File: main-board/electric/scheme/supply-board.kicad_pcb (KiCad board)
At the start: 2 copper layers, 85 x 56 mm, 139 parts, among them K1 CONN_3, P1 PWR-IN, P10 TST, P11 TST, P12 PWR-IN, P13 CONN_4, P14 PWR-IN, P16 TST, P17 TST, P18 TST, P19 TST, P2 PWR-IN, P3 CONN_4, P4 cross board conn, P5 PWR-IN, P6 TST, P7 TST, P8 TST, P9 CONN_3X2, Q1 BC847, Q10 MOS_N, Q11 MOS_P, Q12 MOS_P, Q2 BC847, Q3 BC847, Q4 MOS_P, Q5 BC847, Q6 BC857, Q7 BC847, Q8 BC857, Q9 BC847, U1 NCP3063, U2 L293, U3 MINI-USB-B, X1 8MHz

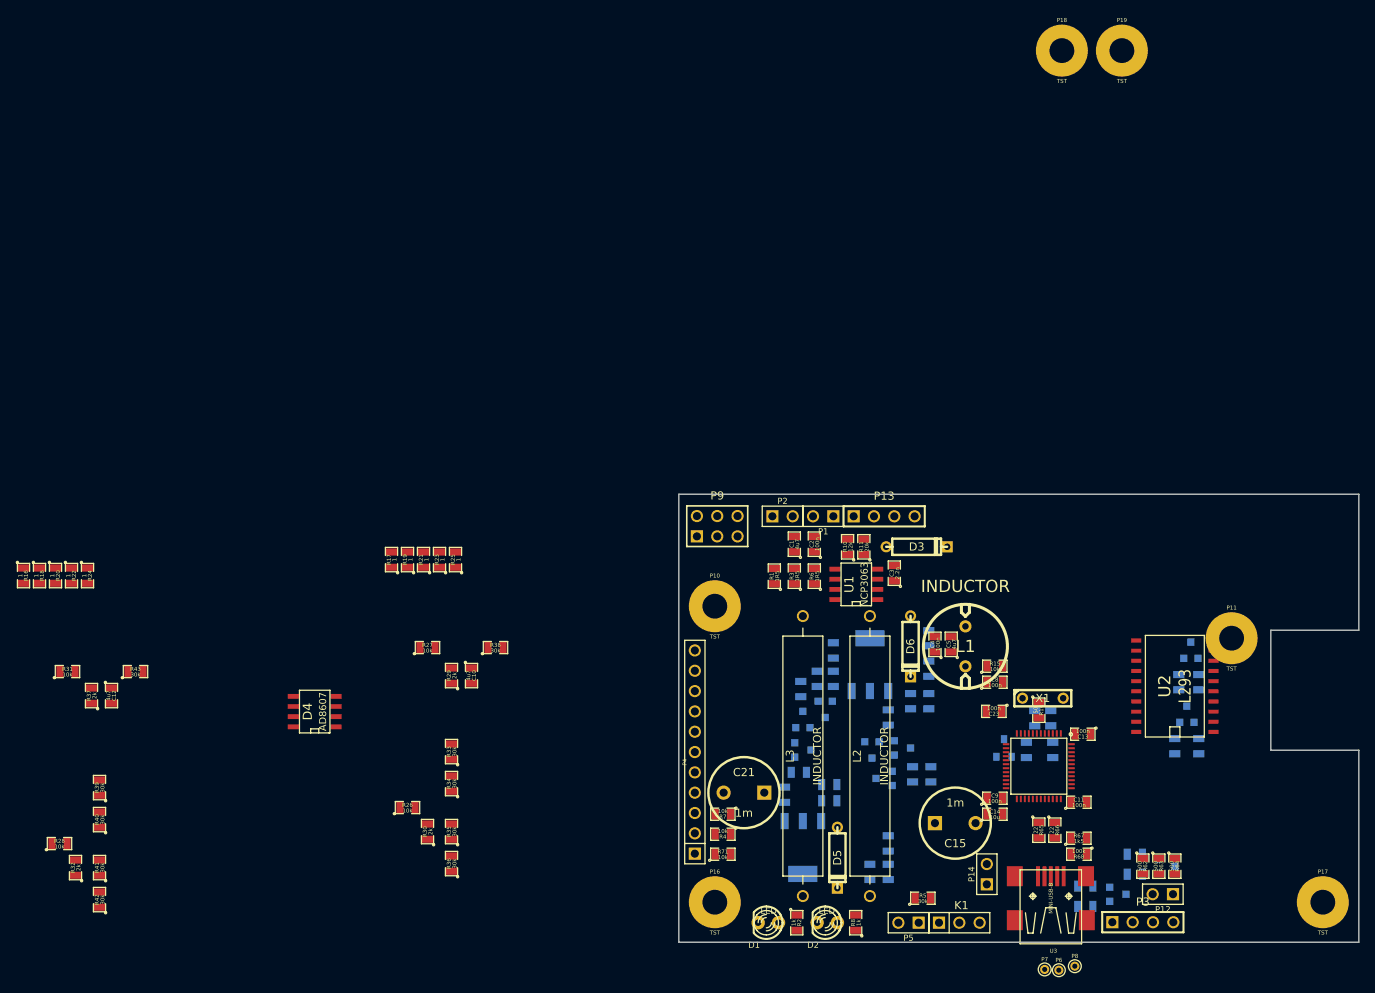
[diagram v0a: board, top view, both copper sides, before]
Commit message: Composed current measure circuit outside of the board.
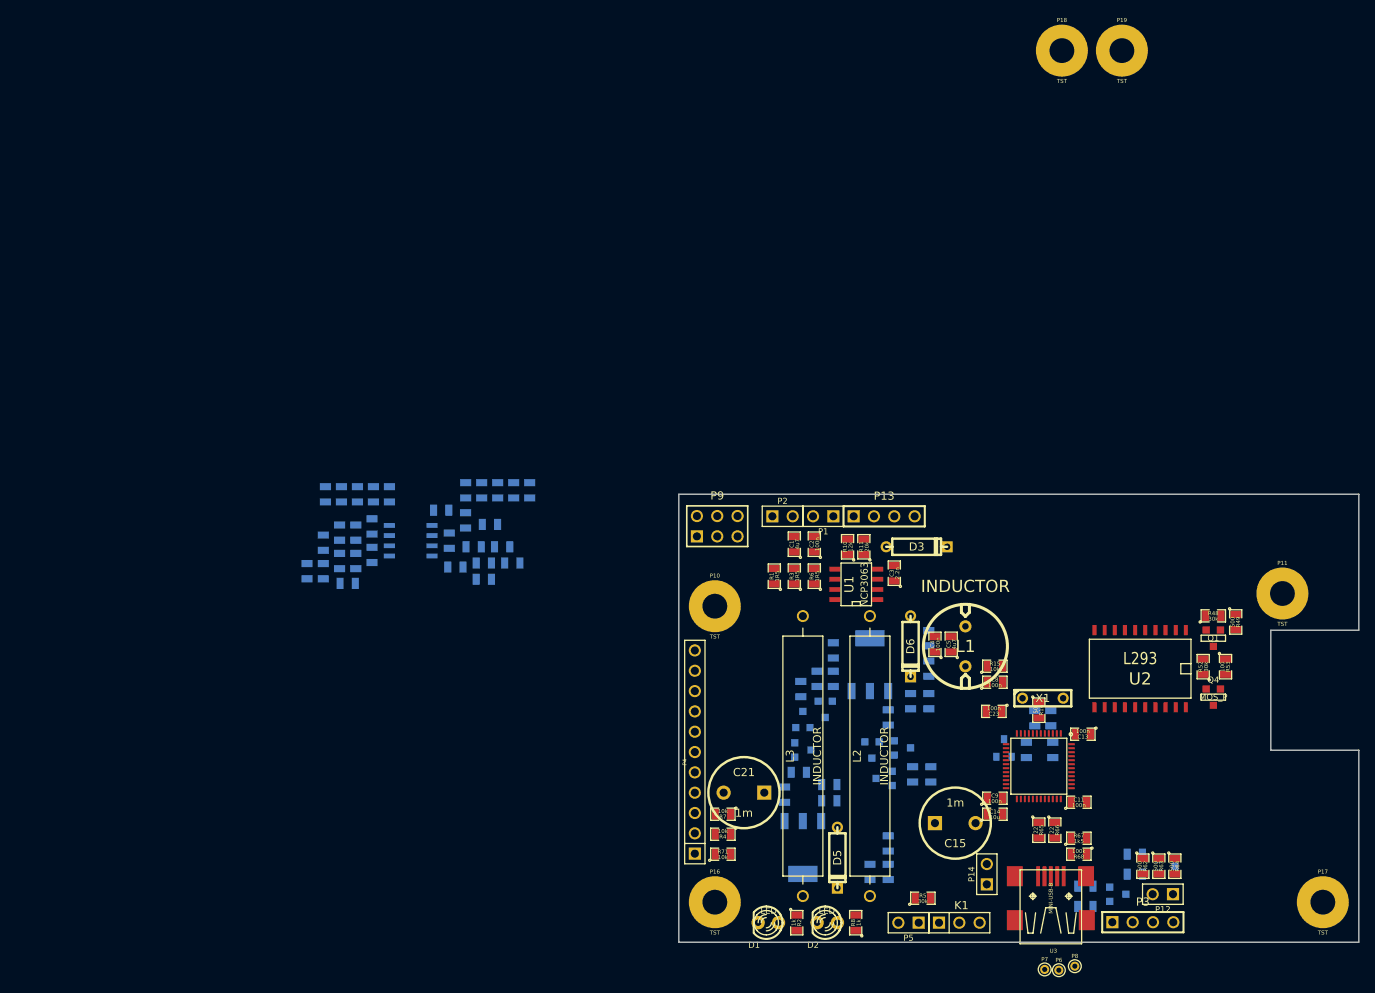
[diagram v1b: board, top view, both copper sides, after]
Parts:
- C10, C12, D4, R16, R17, R18, R19, R20, R21, R22, R23, R24, R25, R26, R27, R28, R29, R30, R31, R32, R33, R34, R35, R36, R37, R38, R39, R40, R41, R42, R43: moved to B.Cu
- Q1, Q4, R48, R49, R52, R53: moved to F.Cu
- moved R32 51.9 mm to (103.1, 133.3)
- moved R42 50.2 mm to (102.1, 136.1), turned to 180 degrees
- moved R28 50.0 mm to (99.1, 131.1), turned to 270 degrees
- moved R41 48.7 mm to (101.1, 133.3)
- moved R16 46.9 mm to (107.3, 125.0)
- moved R18 43.0 mm to (105.3, 125.0)
- moved R40 41.8 mm to (99.1, 134.6), turned to 270 degrees
- moved R36 40.1 mm to (121.4, 131.6), turned to 180 degrees
- moved R31 40.0 mm to (103.1, 129.8), turned to 270 degrees
- moved R20 39.1 mm to (103.3, 125.0)
- moved R39 37.5 mm to (97.0, 134.6)
- moved R37 37.1 mm to (101.1, 129.8), turned to 270 degrees
- moved C12 37.0 mm to (105.2, 132.6)
- moved R35 35.7 mm to (117.9, 131.6), turned to 180 degrees
- moved R22 35.2 mm to (101.3, 125.0)
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
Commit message: Changed USB power from "batt+" to "solar+".
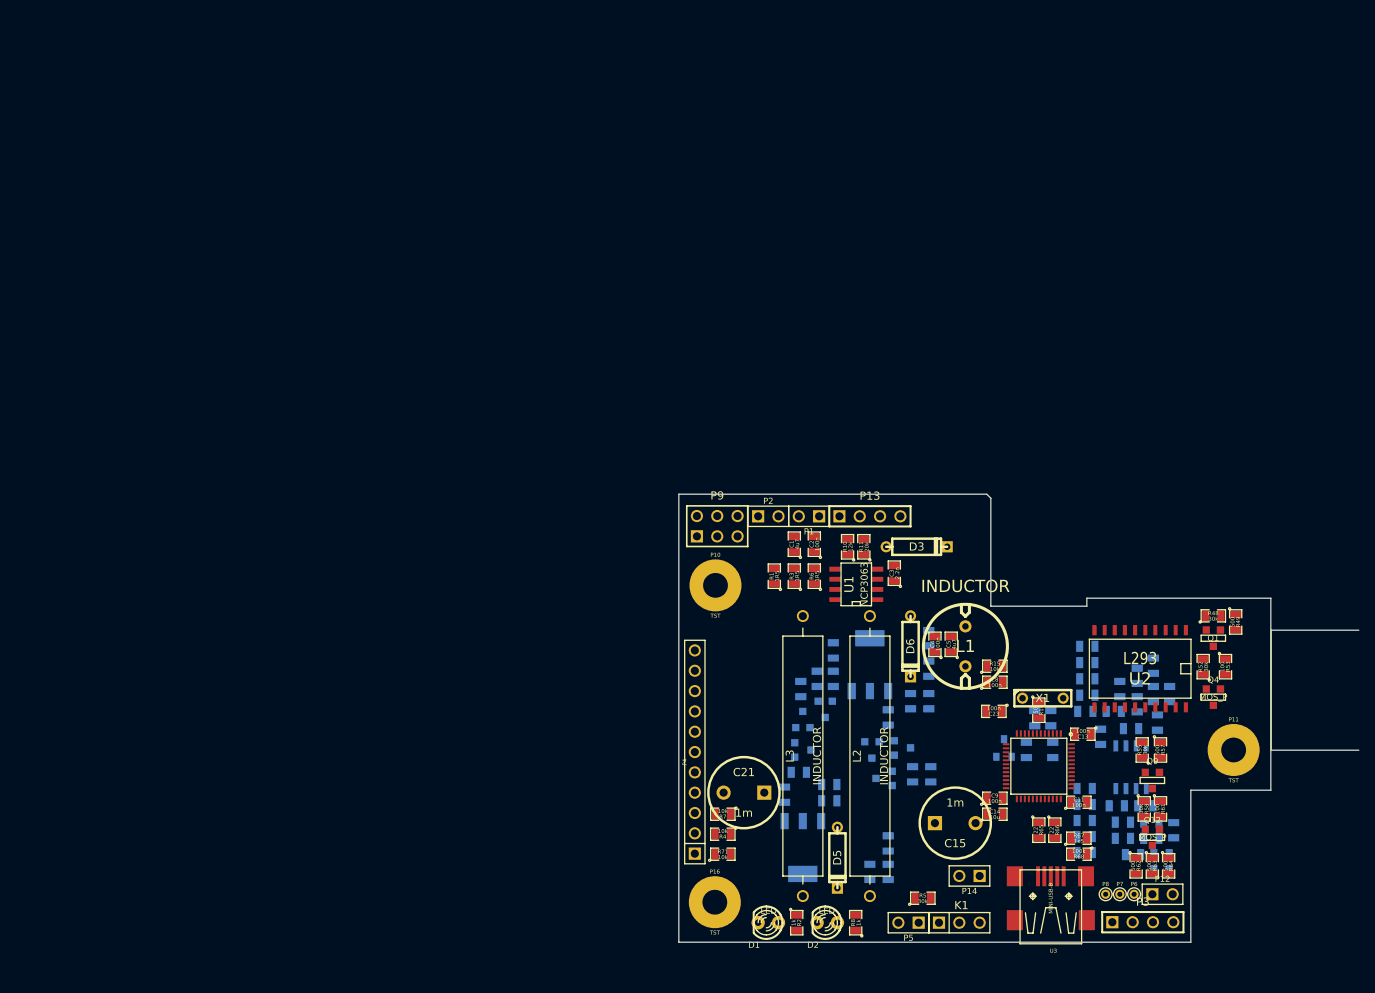
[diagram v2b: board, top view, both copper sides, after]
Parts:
- removed P17, P18, P19: TST, m3-screw-hole
- Q12, Q9, R55, R57, R58, R61: moved to F.Cu
- moved R39 113.2 mm to (203.8, 172.1), turned to 180 degrees
- moved R40 110.6 mm to (203.8, 170.1), turned to 0 degrees
- moved R28 108.5 mm to (200.3, 170.1), turned to 0 degrees
- moved R42 107.8 mm to (205.4, 167.0), turned to 270 degrees
- moved R41 107.2 mm to (202.6, 168.0), turned to 180 degrees
- moved R37 105.1 mm to (199.0, 168.0), turned to 0 degrees
- moved R24 104.9 mm to (194.2, 169.8), turned to 0 degrees
- moved R32 104.7 mm to (202.6, 166.0), turned to 180 degrees
- moved R31 102.5 mm to (199.0, 166.0), turned to 0 degrees
- moved R22 102.3 mm to (194.2, 167.8), turned to 0 degrees
- moved C12 101.6 mm to (201.8, 164.0), turned to 0 degrees
- moved R20 99.6 mm to (194.2, 165.8), turned to 0 degrees
- moved R43 99.4 mm to (198.2, 164.0), turned to 0 degrees
- moved R18 97.0 mm to (194.2, 163.8), turned to 0 degrees
- moved D4 94.4 mm to (200.0, 159.1), turned to 0 degrees
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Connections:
- P14 pad 2: +6V -> /solar+
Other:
- outline, holes or cut-outs redrawn
- net class Default: trace_width 0.2 -> 0.25

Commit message: Routing.
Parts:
- moved P6 5.03 mm to (196.8, 171.4)
- moved C15 3.61 mm to (174.6, 167.3)
- moved P7 2.51 mm to (196.8, 173.2)
- moved R8 1.27 mm to (166.9, 178.6), turned to 180 degrees
- moved R14 1.06 mm to (188.5, 150.9)
- moved X1 1.02 mm to (189.0, 149.5)
- moved D1 0.76 mm to (153.9, 178.6)
- moved D2 0.76 mm to (162.8, 178.6)
- moved C23 0.68 mm to (183.4, 151.7), turned to 0 degrees
- moved R67 0.62 mm to (193.5, 167.4)
- moved R5 0.53 mm to (173.5, 175.4), turned to 90 degrees
- moved R2 0.25 mm to (158.0, 178.6), turned to 180 degrees
- moved C9 0.06 mm to (183.0, 162.9), turned to 180 degrees
- turned C14 to 180 degrees
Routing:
- net GND: track 0.00 -> 83.6 mm
- net +6V: track 0.00 -> 19.1 mm
- net /swd-io: track 0.00 -> 14.2 mm
- net /swd-clk: track 0.00 -> 13.4 mm
- net N-0000044: track 0.00 -> 10.1 mm
- net /usb-connected: track 0.00 -> 8.59 mm
- net N-0000012: track 0.00 -> 7.34 mm
- net N-0000021: track 0.00 -> 6.67 mm
- net N-0000022: track 0.00 -> 5.65 mm
- net N-0000013: track 0.00 -> 5.09 mm
- net N-0000084: track 0.00 -> 4.38 mm
- net N-0000033: track 0.00 -> 4.12 mm
- net VDD: track 0.00 -> 4.01 mm
- net N-0000023: track 0.00 -> 3.62 mm
- net /d+: track 0.00 -> 3.26 mm
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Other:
- board size 85 x 56 mm -> 74 x 56 mm

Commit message: Routing...
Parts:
- moved C23 1.23 mm to (184.6, 152.0)
- moved C12 0.76 mm to (202.6, 164.0)
- moved R43 0.76 mm to (199.0, 164.0), turned to 180 degrees
- turned C13 to 0 degrees
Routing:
- net +6V: track 19.1 -> 103.6 mm
- net GND: track 83.6 -> 157.3 mm
- net /buck-out-5v: track 2.54 -> 53.8 mm
- net /solar+: track 0.00 -> 39.2 mm
- net N-0000026: track 0.00 -> 23.4 mm
- net VDD: track 4.01 -> 21.4 mm
- net N-0000027: track 0.00 -> 13.7 mm
- net /in2+: track 0.00 -> 11.5 mm
- net /solar: track 0.00 -> 11.2 mm
- net /boost+: track 0.00 -> 11.0 mm
- net N-0000017: track 2.00 -> 10.3 mm
- net /in2-: track 0.00 -> 7.90 mm
- net N-0000019: track 0.00 -> 7.00 mm
- net N-000007: track 0.00 -> 5.09 mm
- net N-0000034: track 0.00 -> 5.04 mm
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
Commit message: Routing...
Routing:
- net N-000008: track 0.00 -> 12.9 mm
- net /in1+: track 0.00 -> 10.9 mm
- net GND: track 157.3 -> 167.8 mm
- net /buck+: track 0.00 -> 9.88 mm
- net /in1-: track 0.00 -> 9.36 mm
- net +6V: track 103.6 -> 111.8 mm
- net N-0000014: track 0.00 -> 5.38 mm
- net N-0000020: track 2.31 -> 5.52 mm
- net N-0000019: track 7.00 -> 10.2 mm
- net /buck-current: track 0.00 -> 1.98 mm
- net N-0000059: track 0.00 -> 1.65 mm
- net N-0000058: track 0.00 -> 1.65 mm

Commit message: Routing...
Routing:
- net GND: track 167.8 -> 257.9 mm
- net /buck+: track 9.88 -> 20.0 mm
- net /buck-out-5v: track 53.8 -> 63.3 mm
- net N-000003: track 4.73 -> 14.1 mm
- net N-000007: track 5.09 -> 14.5 mm
- net N-000002: track 0.00 -> 8.99 mm
- net N-000004: track 0.00 -> 8.43 mm
- net +6V: track 111.8 -> 118.5 mm
- net /solar: track 11.2 -> 15.6 mm
- net N-000006: track 0.00 -> 4.24 mm
- net VDD: track 21.4 -> 24.1 mm
- net N-000005: track 0.00 -> 2.40 mm
- net N-0000015: track 0.00 -> 2.35 mm
- net N-000001: track 0.00 -> 2.35 mm
- net /batt-volt: track 0.00 -> 1.91 mm
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
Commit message: Routing...
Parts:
- moved U2 13.0 mm to (206.5, 135.0), turned to 90 degrees
- moved R48 11.8 mm to (201.5, 147.9), turned to 90 degrees
- moved R49 11.7 mm to (202.2, 145.1), turned to 0 degrees
- moved Q1 7.82 mm to (204.3, 147.9), turned to 90 degrees
- moved R53 4.03 mm to (207.8, 146.4), turned to 0 degrees
- moved R52 2.92 mm to (207.8, 149.2), turned to 180 degrees
- moved Q4 2.76 mm to (211.6, 147.9), turned to 90 degrees
- moved C14 1.21 mm to (181.8, 164.9)
- moved R65 0.56 mm to (188.8, 167.5)
- moved R66 0.50 mm to (190.5, 167.5)
- moved R28 0.38 mm to (200.3, 170.4)
- moved R39 0.25 mm to (203.8, 172.3)
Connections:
- stm1 pad 25: /light -> (no net)
- stm1 pad 26: /moto4 -> /led1
- stm1 pad 27: /moto3 -> /led2
- stm1 pad 29: (no net) -> /usb-connected
- stm1 pad 3: /led1 -> /moto4
- stm1 pad 38: /usb-connected -> (no net)
- stm1 pad 4: /led2 -> /moto3
- stm1 pad 41: (no net) -> /light
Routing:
- net GND: track 257.9 -> 363.1 mm
- net /wakeup: track 0.00 -> 40.3 mm
- net /sda-int: track 2.59 -> 42.9 mm, vias 0 -> 2
- net /scl-int: track 2.61 -> 42.1 mm, vias 0 -> 2
- net /moto-en: track 1.92 -> 39.7 mm, vias 0 -> 2
- net /led1: track 0.00 -> 35.9 mm
- net /moto3: track 0.00 -> 33.2 mm
- net /buck-pwm: track 0.00 -> 32.8 mm, vias 0 -> 1
- net /led2: track 0.00 -> 28.1 mm
- net /rx: track 0.00 -> 27.4 mm
- net /tx: track 0.00 -> 23.6 mm
- net /moto4: track 0.00 -> 23.5 mm
- net /just-power-source: track 2.22 -> 25.0 mm
- net /boost-pwm: track 0.00 -> 17.7 mm, vias 0 -> 1
- net N-0000011: track 0.00 -> 15.9 mm
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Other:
- outline, holes or cut-outs redrawn

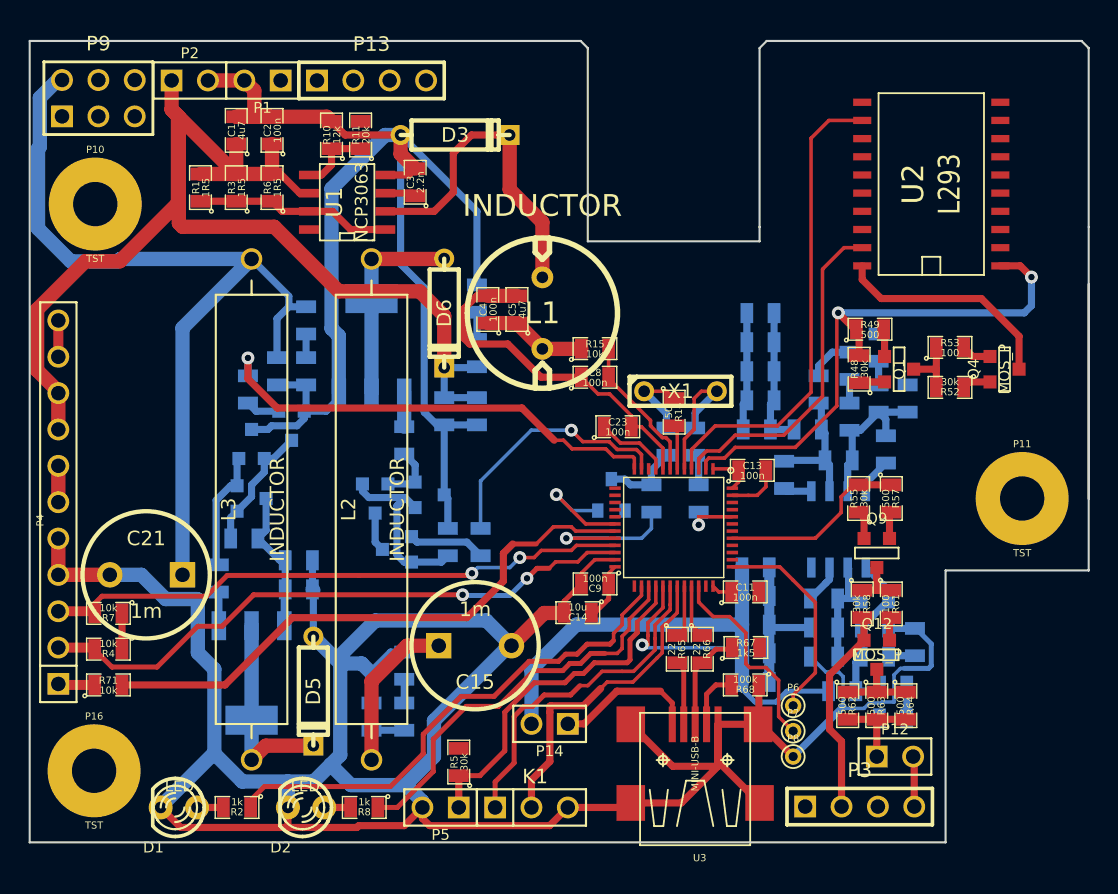
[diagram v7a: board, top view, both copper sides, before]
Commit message: Routing and changing netlist to make routing more convenient.
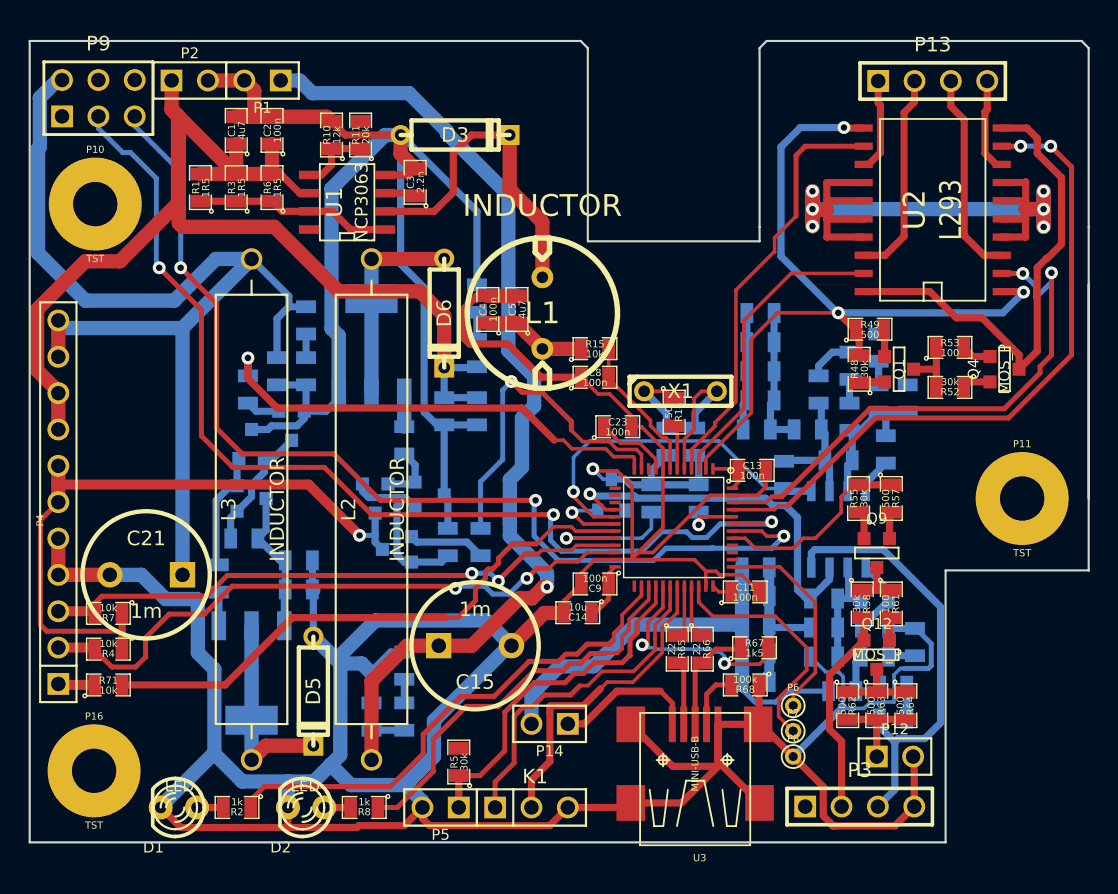
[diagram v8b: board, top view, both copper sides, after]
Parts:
- moved P13 39.2 mm to (206.6, 127.8)
- moved U2 1.80 mm to (206.6, 136.8)
- moved R67 0.60 mm to (194.2, 167.4)
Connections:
- P13 pad 1: /out2 -> /out4
- P13 pad 2: /out1 -> /out3
- P13 pad 3: /out4 -> /out1
- P13 pad 4: /out3 -> /out2
- stm1 pad 45: /moto1 -> /moto2
- stm1 pad 46: /moto2 -> /moto1
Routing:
- net GND: track 363.1 -> 471.2 mm, vias 0 -> 7
- net /scl-rpi: track 0.00 -> 77.0 mm, vias 0 -> 3
- net /sda-rpi: track 0.00 -> 74.2 mm, vias 0 -> 3
- net VDD: track 29.1 -> 98.4 mm, vias 0 -> 1
- net /solar: track 15.6 -> 74.1 mm, vias 0 -> 1
- net /moto2: track 0.00 -> 46.8 mm, vias 0 -> 2
- net /moto1: track 0.00 -> 38.3 mm, vias 0 -> 2
- net /boost-current: track 2.71 -> 26.3 mm, vias 0 -> 1
- net /buck-current: track 1.98 -> 24.8 mm, vias 0 -> 1
- net N-0000011: track 15.9 -> 34.6 mm
- net /moto-en: track 39.7 -> 55.7 mm, vias 2 -> 3
- net /out3: track 0.00 -> 14.5 mm
- net /out1: track 0.00 -> 14.4 mm
- net /buck-out-5v: track 63.3 -> 75.5 mm
- net /out2: track 0.00 -> 6.61 mm
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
